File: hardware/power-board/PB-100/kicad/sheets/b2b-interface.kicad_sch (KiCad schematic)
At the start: 0 parts

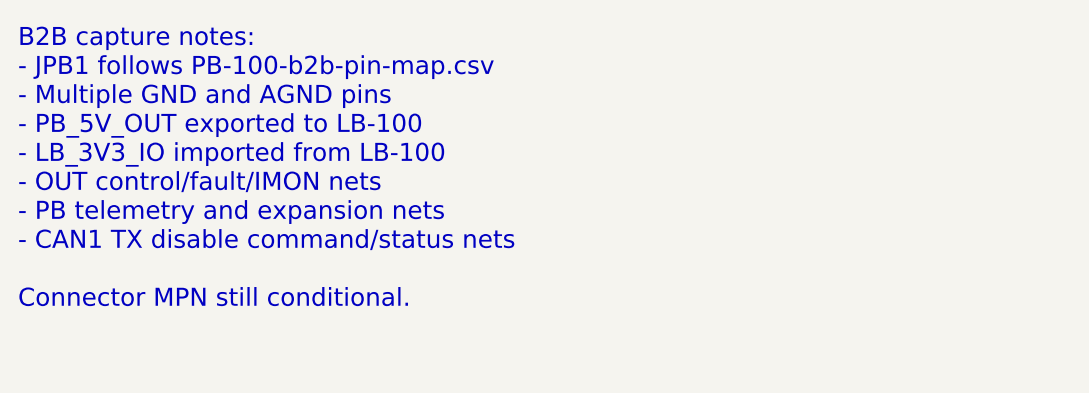
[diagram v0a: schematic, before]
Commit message: hardware: select pb100 jpb1 connector candidate
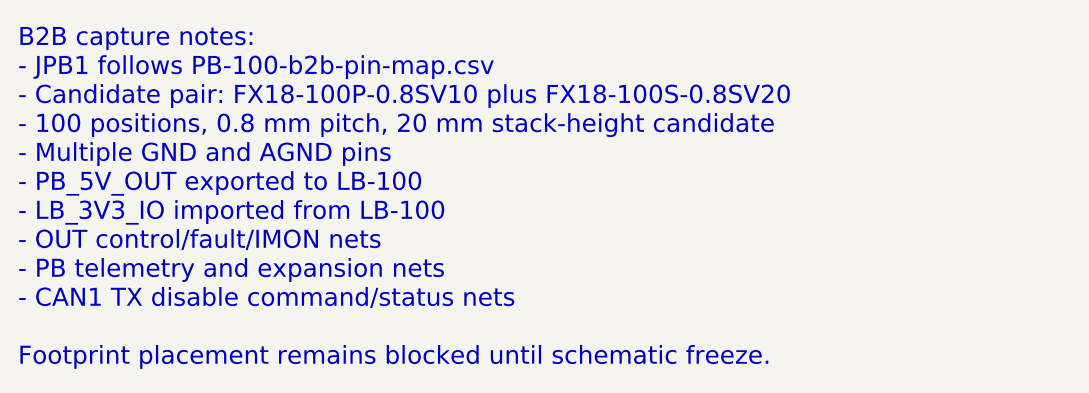
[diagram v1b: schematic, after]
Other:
- note added: "B2B capture notes: - JPB1 follows PB-100-b2b-pin-map.csv - Candidate pair: FX18-100P-0.8SV10 plus FX18-100S-0.8SV20 - 100 positions, 0.8 mm pitch, 20 mm stack-height candidate - Multiple GND and AGND pins - PB_5V_OUT exported to LB-100 - LB_3V3_IO imported from LB-100 - OUT control/fault/IMON nets - PB telemetry and expansion nets - CAN1 TX disable command/status nets Footprint placement remains 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"
- note removed: "B2B capture notes: - JPB1 follows PB-100-b2b-pin-map.csv - Multiple GND and AGND pins - PB_5V_OUT exported to LB-100 - LB_3V3_IO imported from LB-100 - OUT control/fault/IMON nets - PB telemetry and expansion nets - CAN1 TX disable command/status nets Connector MPN still conditional."
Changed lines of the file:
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@@
     (company "SVC Platform")
     (comment 9 "Work queue: CAP-B2B. B2B capture follows JPB1 pin map.")
-    (comment 1 "Placeholder sheet. Capture JPB1 100-pin interface here.")
+    (comment 1 "Placeholder sheet. Capture JPB1 100-pin FX18 candidate interface here.")
     (comment 2 "Source: PB-100-b2b-pin-map.csv.")
   )
-  (text "B2B capture notes:\n- JPB1 follows PB-100-b2b-pin-map.csv\n- Multiple GND and AGND pins\n- PB_5V_OUT exported to LB-100\n- LB_3V3_IO imported from LB-100\n- OUT control/fault/IMON nets\n- PB telemetry and expansion nets\n- CAN1 TX disable command/status nets\n\nConnector MPN still conditional."
+  (text "B2B capture notes:\n- JPB1 follows PB-100-b2b-pin-map.csv\n- Candidate pair: FX18-100P-0.8SV10 plus FX18-100S-0.8SV20\n- 100 positions, 0.8 mm pitch, 20 mm stack-height candidate\n- Multiple GND and AGND pins\n- PB_5V_OUT exported to LB-100\n- LB_3V3_IO imported from LB-100\n- OUT control/fault/IMON nets\n- PB telemetry and expansion nets\n- CAN1 TX disable command/status nets\n\nFootprint placement remains blocked until schematic freeze."
     (at 25 30 0)
     (effects (font (size 2.0 2.0)) (justify left top))

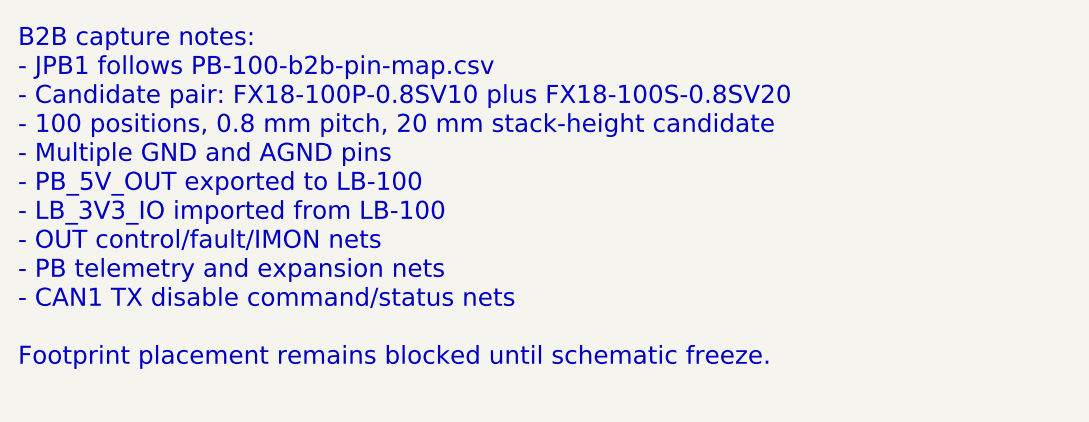
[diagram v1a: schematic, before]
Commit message: hardware: sync pb100 kicad sheet trace notes
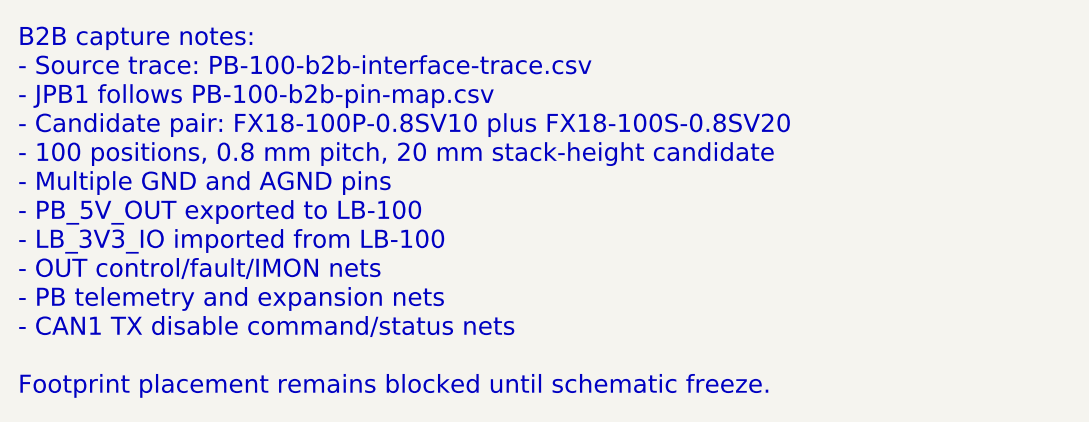
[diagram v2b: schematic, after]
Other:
- note added: "B2B capture notes: - Source trace: PB-100-b2b-interface-trace.csv - JPB1 follows PB-100-b2b-pin-map.csv - Candidate pair: FX18-100P-0.8SV10 plus FX18-100S-0.8SV20 - 100 positions, 0.8 mm pitch, 20 mm stack-height candidate - Multiple GND and AGND pins - PB_5V_OUT exported to LB-100 - LB_3V3_IO imported from LB-100 - OUT control/fault/IMON nets - PB telemetry and expansion nets - CAN1 TX disable c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"
- note removed: "B2B capture notes: - JPB1 follows PB-100-b2b-pin-map.csv - Candidate pair: FX18-100P-0.8SV10 plus FX18-100S-0.8SV20 - 100 positions, 0.8 mm pitch, 20 mm stack-height candidate - Multiple GND and AGND pins - PB_5V_OUT exported to LB-100 - LB_3V3_IO imported from LB-100 - OUT control/fault/IMON nets - PB telemetry and expansion nets - CAN1 TX disable command/status nets Footprint placement remains 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"
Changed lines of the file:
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@@
     (comment 9 "Work queue: CAP-B2B. B2B capture follows JPB1 pin map.")
     (comment 1 "Placeholder sheet. Capture JPB1 100-pin FX18 candidate interface here.")
-    (comment 2 "Source: PB-100-b2b-pin-map.csv.")
+    (comment 2 "Sources: PB-100-b2b-interface-trace.csv and PB-100-b2b-pin-map.csv.")
   )
-  (text "B2B capture notes:\n- JPB1 follows PB-100-b2b-pin-map.csv\n- Candidate pair: FX18-100P-0.8SV10 plus FX18-100S-0.8SV20\n- 100 positions, 0.8 mm pitch, 20 mm stack-height candidate\n- Multiple GND and AGND pins\n- PB_5V_OUT exported to LB-100\n- LB_3V3_IO imported from LB-100\n- OUT control/fault/IMON nets\n- PB telemetry and expansion nets\n- CAN1 TX disable command/status nets\n\nFootprint placement remains blocked until schematic freeze."
+  (text "B2B capture notes:\n- Source trace: PB-100-b2b-interface-trace.csv\n- JPB1 follows PB-100-b2b-pin-map.csv\n- Candidate pair: FX18-100P-0.8SV10 plus FX18-100S-0.8SV20\n- 100 positions, 0.8 mm pitch, 20 mm stack-height candidate\n- Multiple GND and AGND pins\n- PB_5V_OUT exported to LB-100\n- LB_3V3_IO imported from LB-100\n- OUT control/fault/IMON nets\n- PB telemetry and expansion nets\n- CAN1 TX disable command/status nets\n\nFootprint placement remains blocked until schematic freeze."
     (at 25 30 0)
     (effects (font (size 2.0 2.0)) (justify left top))

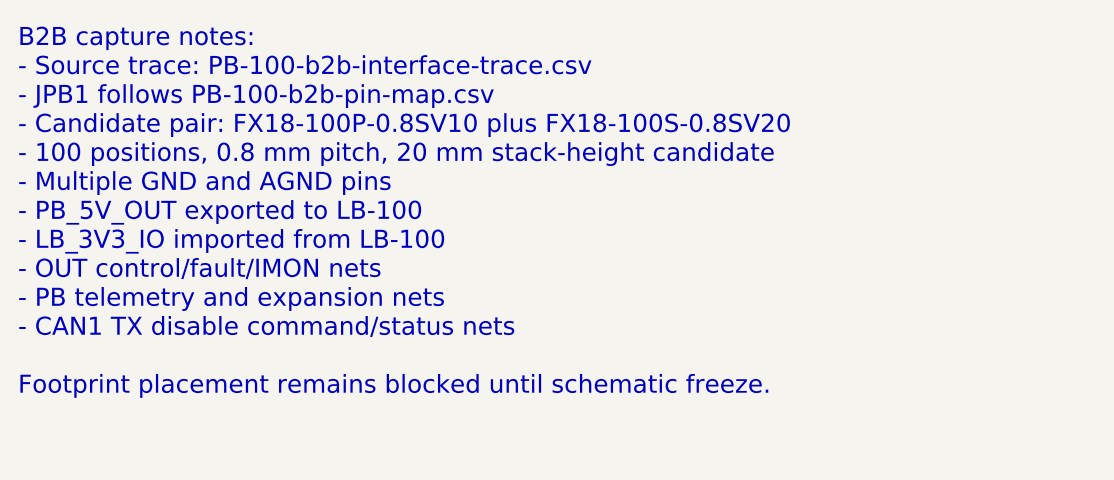
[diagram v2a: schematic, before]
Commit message: hardware: add pb100 b2b resource binding
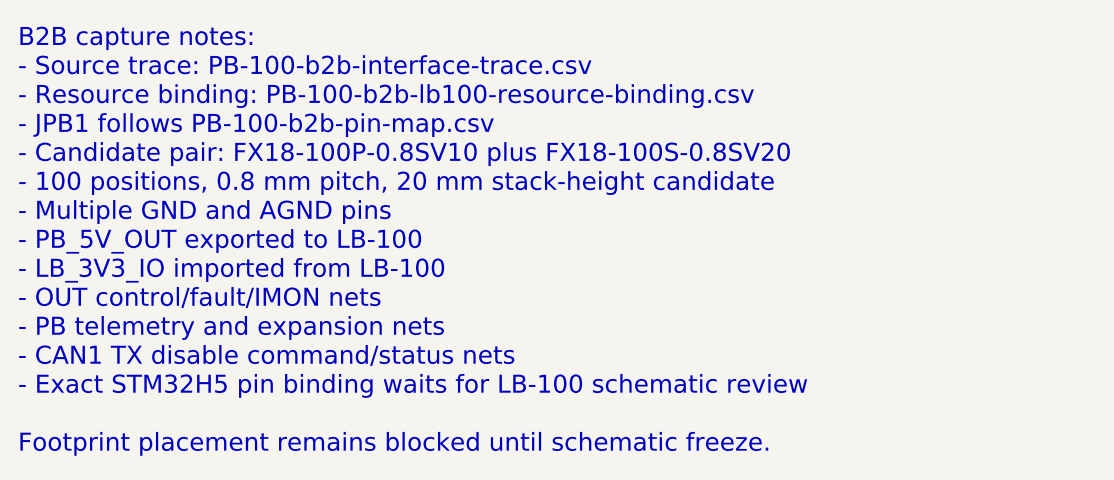
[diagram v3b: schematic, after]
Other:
- note added: "B2B capture notes: - Source trace: PB-100-b2b-interface-trace.csv - Resource binding: PB-100-b2b-lb100-resource-binding.csv - JPB1 follows PB-100-b2b-pin-map.csv - Candidate pair: FX18-100P-0.8SV10 plus FX18-100S-0.8SV20 - 100 positions, 0.8 mm pitch, 20 mm stack-height candidate - Multiple GND and AGND pins - PB_5V_OUT exported to LB-100 - LB_3V3_IO imported from LB-100 - OUT control/fault/IMON 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"
- note removed: "B2B capture notes: - Source trace: PB-100-b2b-interface-trace.csv - JPB1 follows PB-100-b2b-pin-map.csv - Candidate pair: FX18-100P-0.8SV10 plus FX18-100S-0.8SV20 - 100 positions, 0.8 mm pitch, 20 mm stack-height candidate - Multiple GND and AGND pins - PB_5V_OUT exported to LB-100 - LB_3V3_IO imported from LB-100 - OUT control/fault/IMON nets - PB telemetry and expansion nets - CAN1 TX disable c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"
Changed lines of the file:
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@@
     (comment 9 "Work queue: CAP-B2B. B2B capture follows JPB1 pin map.")
     (comment 1 "Placeholder sheet. Capture JPB1 100-pin FX18 candidate interface here.")
-    (comment 2 "Sources: PB-100-b2b-interface-trace.csv and PB-100-b2b-pin-map.csv.")
+    (comment 2 "Sources: PB-100-b2b-interface-trace.csv, PB-100-b2b-lb100-resource-binding.csv, and PB-100-b2b-pin-map.csv.")
   )
-  (text "B2B capture notes:\n- Source trace: PB-100-b2b-interface-trace.csv\n- JPB1 follows PB-100-b2b-pin-map.csv\n- Candidate pair: FX18-100P-0.8SV10 plus FX18-100S-0.8SV20\n- 100 positions, 0.8 mm pitch, 20 mm stack-height candidate\n- Multiple GND and AGND pins\n- PB_5V_OUT exported to LB-100\n- LB_3V3_IO imported from LB-100\n- OUT control/fault/IMON nets\n- PB telemetry and expansion nets\n- CAN1 TX disable command/status nets\n\nFootprint placement remains blocked until schematic freeze."
+  (text "B2B capture notes:\n- Source trace: PB-100-b2b-interface-trace.csv\n- Resource binding: PB-100-b2b-lb100-resource-binding.csv\n- JPB1 follows PB-100-b2b-pin-map.csv\n- Candidate pair: FX18-100P-0.8SV10 plus FX18-100S-0.8SV20\n- 100 positions, 0.8 mm pitch, 20 mm stack-height candidate\n- Multiple GND and AGND pins\n- PB_5V_OUT exported to LB-100\n- LB_3V3_IO imported from LB-100\n- OUT control/fault/IMON nets\n- PB telemetry and expansion nets\n- CAN1 TX disable command/status nets\n- Exact STM32H5 pin binding waits for LB-100 schematic review\n\nFootprint placement remains blocked until schematic freeze."
     (at 25 30 0)
     (effects (font (size 2.0 2.0)) (justify left top))

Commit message: Capture preliminary PB-100 schematic sheets
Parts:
- added JPB1: JPB1_100PIN_PRELIM, symbol PB100:PB100_JPB1_100PIN_PRELIM
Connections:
- new net ADC_REF: JPB1.66 (ADC_REF)
- new net AGND: JPB1.11 (AGND), JPB1.12 (AGND)
- new net CAN1_RX_ROUTE: JPB1.69 (CAN1_RX_ROUTE)
- new net CAN1_TX_DISABLED_STATUS: JPB1.68 (CAN1_TX_DISABLED_STATUS)
- new net CAN1_TX_DISABLE_CMD: JPB1.67 (CAN1_TX_DISABLE_CMD)
- new net CAN1_TX_ROUTE: JPB1.70 (CAN1_TX_ROUTE)
- new net CAN2_RX_ROUTE: JPB1.71 (CAN2_RX_ROUTE)
- new net CAN2_TX_ROUTE: JPB1.72 (CAN2_TX_ROUTE)
- new net EXT_5V_EN: JPB1.84 (EXT_5V_EN)
- new net EXT_ADC1: JPB1.80 (EXT_ADC1)
- new net EXT_ADC2: JPB1.81 (EXT_ADC2)
- new net EXT_DIG1: JPB1.82 (EXT_DIG1)
- new net EXT_DIG2: JPB1.83 (EXT_DIG2)
- new net GND: JPB1.1 (GND), JPB1.10 (GND), JPB1.2 (GND), JPB1.3 (GND), JPB1.4 (GND), JPB1.5 (GND), JPB1.6 (GND), JPB1.7 (GND), JPB1.8 (GND), JPB1.9 (GND)
- new net IIN_SENSE: JPB1.52 (IIN_SENSE)
- new net LB_3V3_IO: JPB1.17 (LB_3V3_IO), JPB1.18 (LB_3V3_IO)
- new net LIN_RX: JPB1.74 (LIN_RX)
- new net LIN_TX: JPB1.73 (LIN_TX)
- new net OUT10_CTL: JPB1.30 (OUT10_CTL)
- new net OUT10_FLT: JPB1.40 (OUT10_FLT)
- new net OUT10_IMON: JPB1.50 (OUT10_IMON)
- new net OUT1_CTL: JPB1.21 (OUT1_CTL)
- new net OUT1_FLT: JPB1.31 (OUT1_FLT)
- new net OUT1_IMON: JPB1.41 (OUT1_IMON)
- new net OUT2_CTL: JPB1.22 (OUT2_CTL)
- new net OUT2_FLT: JPB1.32 (OUT2_FLT)
- new net OUT2_IMON: JPB1.42 (OUT2_IMON)
- new net OUT3_CTL: JPB1.23 (OUT3_CTL)
- new net OUT3_FLT: JPB1.33 (OUT3_FLT)
- new net OUT3_IMON: JPB1.43 (OUT3_IMON)
- new net OUT4_CTL: JPB1.24 (OUT4_CTL)
- new net OUT4_FLT: JPB1.34 (OUT4_FLT)
- new net OUT4_IMON: JPB1.44 (OUT4_IMON)
- new net OUT5_CTL: JPB1.25 (OUT5_CTL)
- new net OUT5_FLT: JPB1.35 (OUT5_FLT)
- new net OUT5_IMON: JPB1.45 (OUT5_IMON)
- new net OUT6_CTL: JPB1.26 (OUT6_CTL)
- new net OUT6_FLT: JPB1.36 (OUT6_FLT)
- new net OUT6_IMON: JPB1.46 (OUT6_IMON)
- new net OUT7_CTL: JPB1.27 (OUT7_CTL)
- new net OUT7_FLT: JPB1.37 (OUT7_FLT)
- new net OUT7_IMON: JPB1.47 (OUT7_IMON)
- new net OUT8_CTL: JPB1.28 (OUT8_CTL)
- new net OUT8_FLT: JPB1.38 (OUT8_FLT)
- new net OUT8_IMON: JPB1.48 (OUT8_IMON)
- new net OUT9_CTL: JPB1.29 (OUT9_CTL)
- new net OUT9_FLT: JPB1.39 (OUT9_FLT)
- new net OUT9_IMON: JPB1.49 (OUT9_IMON)
- new net PB_5V_OUT: JPB1.13 (PB_5V_OUT), JPB1.14 (PB_5V_OUT), JPB1.15 (PB_5V_OUT), JPB1.16 (PB_5V_OUT)
- new net PB_FAULT: JPB1.56 (PB_FAULT)
- new net PB_I2C_INT: JPB1.59 (PB_I2C_INT)
- new net PB_I2C_SCL: JPB1.57 (PB_I2C_SCL)
- new net PB_I2C_SDA: JPB1.58 (PB_I2C_SDA)
- new net PB_ID_ADC: JPB1.60 (PB_ID_ADC)
- new net PB_PWR_GOOD: JPB1.19 (PB_PWR_GOOD)
- new net PB_SPI_CS0: JPB1.64 (PB_SPI_CS0)
- new net PB_SPI_CS1: JPB1.65 (PB_SPI_CS1)
- new net PB_SPI_MISO: JPB1.62 (PB_SPI_MISO)
- new net PB_SPI_MOSI: JPB1.63 (PB_SPI_MOSI)
- new net PB_SPI_SCK: JPB1.61 (PB_SPI_SCK)
- new net PB_WAKE_REQ: JPB1.20 (PB_WAKE_REQ)
- new net RS485_DE: JPB1.75 (RS485_DE)
- new net RS485_RX: JPB1.76 (RS485_RX)
- new net RS485_TX: JPB1.77 (RS485_TX)
- new net SPARE_01: JPB1.85 (SPARE_01)
- new net SPARE_02: JPB1.86 (SPARE_02)
- new net SPARE_03: JPB1.87 (SPARE_03)
- new net SPARE_04: JPB1.88 (SPARE_04)
- new net SPARE_05: JPB1.89 (SPARE_05)
- new net SPARE_06: JPB1.90 (SPARE_06)
- new net SPARE_07: JPB1.91 (SPARE_07)
- new net SPARE_08: JPB1.92 (SPARE_08)
- new net SPARE_09: JPB1.93 (SPARE_09)
- new net SPARE_10: JPB1.94 (SPARE_10)
- new net SPARE_11: JPB1.95 (SPARE_11)
- new net SPARE_12: JPB1.96 (SPARE_12)
- new net SPARE_13: JPB1.97 (SPARE_13)
- new net SPARE_14: JPB1.98 (SPARE_14)
- new net SPARE_15: JPB1.99 (SPARE_15)
- new net SPARE_16: JPB1.100 (SPARE_16)
- new net TEMP_PCB: JPB1.53 (TEMP_PCB)
- new net TEMP_PWR_A: JPB1.54 (TEMP_PWR_A)
- new net TEMP_PWR_B: JPB1.55 (TEMP_PWR_B)
- new net UART_RX: JPB1.79 (UART_RX)
- new net UART_TX: JPB1.78 (UART_TX)
- new net VBAT_SENSE: JPB1.51 (VBAT_SENSE)
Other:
- note added: "B2B interface capture notes: - Source traces: PB-100-b2b-interface-trace.csv, PB-100-b2b-lb100-resource-binding.csv, PB-100-b2b-pin-map.csv, PB-100-b2b-pin-budget.csv - JPB1 candidates FX18-100P-0.8SV10 and FX18-100S-0.8SV20 carry power, output controls, faults, current telemetry, board telemetry, CAN1 safety, and reserves - Exact LB-100 MCU pin binding remains schematic-freeze work No PCB layout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"
- note removed: "B2B capture notes: - Source trace: PB-100-b2b-interface-trace.csv - Resource binding: PB-100-b2b-lb100-resource-binding.csv - JPB1 follows PB-100-b2b-pin-map.csv - Candidate pair: FX18-100P-0.8SV10 plus FX18-100S-0.8SV20 - 100 positions, 0.8 mm pitch, 20 mm stack-height candidate - Multiple GND and AGND pins - PB_5V_OUT exported to LB-100 - LB_3V3_IO imported from LB-100 - OUT control/fault/IMON 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"

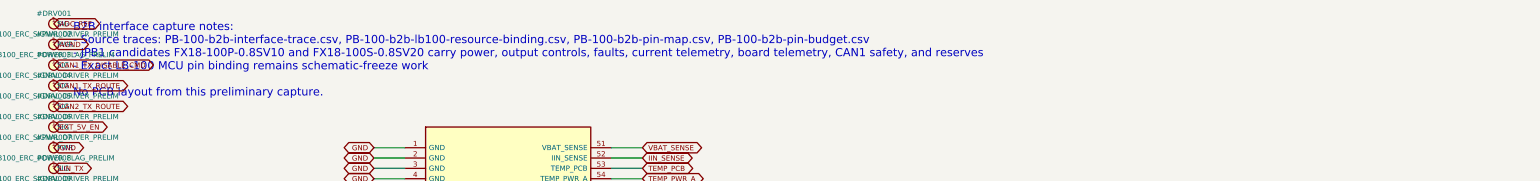
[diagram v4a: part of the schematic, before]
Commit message: Add PB-100 B2B pin audit checklist
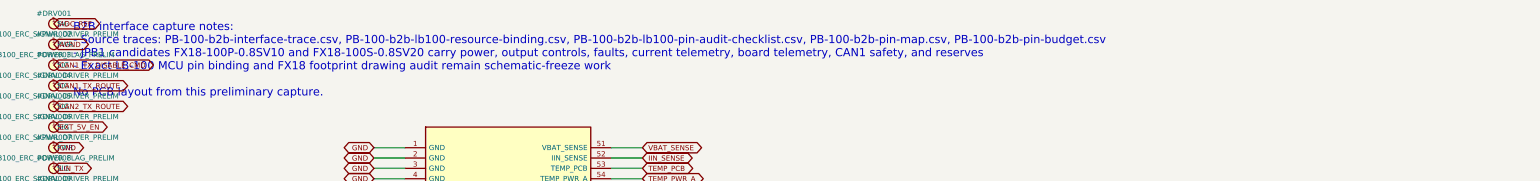
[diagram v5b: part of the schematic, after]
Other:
- note added: "B2B interface capture notes: - Source traces: PB-100-b2b-interface-trace.csv, PB-100-b2b-lb100-resource-binding.csv, PB-100-b2b-lb100-pin-audit-checklist.csv, PB-100-b2b-pin-map.csv, PB-100-b2b-pin-budget.csv - JPB1 candidates FX18-100P-0.8SV10 and FX18-100S-0.8SV20 carry power, output controls, faults, current telemetry, board telemetry, CAN1 safety, and reserves - Exact LB-100 MCU pin binding a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"
- note removed: "B2B interface capture notes: - Source traces: PB-100-b2b-interface-trace.csv, PB-100-b2b-lb100-resource-binding.csv, PB-100-b2b-pin-map.csv, PB-100-b2b-pin-budget.csv - JPB1 candidates FX18-100P-0.8SV10 and FX18-100S-0.8SV20 carry power, output controls, faults, current telemetry, board telemetry, CAN1 safety, and reserves - Exact LB-100 MCU pin binding remains schematic-freeze work No PCB layout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"
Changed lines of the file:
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@@
     (comment 9 "Work queue: CAP-B2B. Preliminary schematic capture follows PB-100-schematic-capture-work-queue.csv.")
     (comment 1 "Preliminary capture for JPB1 100-pin FX18 candidate interface.")
-    (comment 2 "Sources: PB-100-b2b-interface-trace.csv, PB-100-b2b-lb100-resource-binding.csv, and PB-100-b2b-pin-map.csv.")
+    (comment 2 "Sources: PB-100-b2b-interface-trace.csv, PB-100-b2b-lb100-resource-binding.csv, PB-100-b2b-lb100-pin-audit-checklist.csv, and PB-100-b2b-pin-map.csv.")
   )
-  (text "B2B interface capture notes:\n- Source traces: PB-100-b2b-interface-trace.csv, PB-100-b2b-lb100-resource-binding.csv, PB-100-b2b-pin-map.csv, PB-100-b2b-pin-budget.csv\n- JPB1 candidates FX18-100P-0.8SV10 and FX18-100S-0.8SV20 carry power, output controls, faults, current telemetry, board telemetry, CAN1 safety, and reserves\n- Exact LB-100 MCU pin binding remains schematic-freeze work\n\nNo PCB layout from this preliminary capture."
+  (text "B2B interface capture notes:\n- Source traces: PB-100-b2b-interface-trace.csv, PB-100-b2b-lb100-resource-binding.csv, PB-100-b2b-lb100-pin-audit-checklist.csv, PB-100-b2b-pin-map.csv, PB-100-b2b-pin-budget.csv\n- JPB1 candidates FX18-100P-0.8SV10 and FX18-100S-0.8SV20 carry power, output controls, faults, current telemetry, board telemetry, CAN1 safety, and reserves\n- Exact LB-100 MCU pin binding and FX18 footprint drawing audit remain schematic-freeze work\n\nNo PCB layout from this preliminary capture."
     (at 20 20 0)
     (effects (font (size 2.0 2.0)) (justify left top))
